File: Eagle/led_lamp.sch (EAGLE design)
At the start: 7 parts

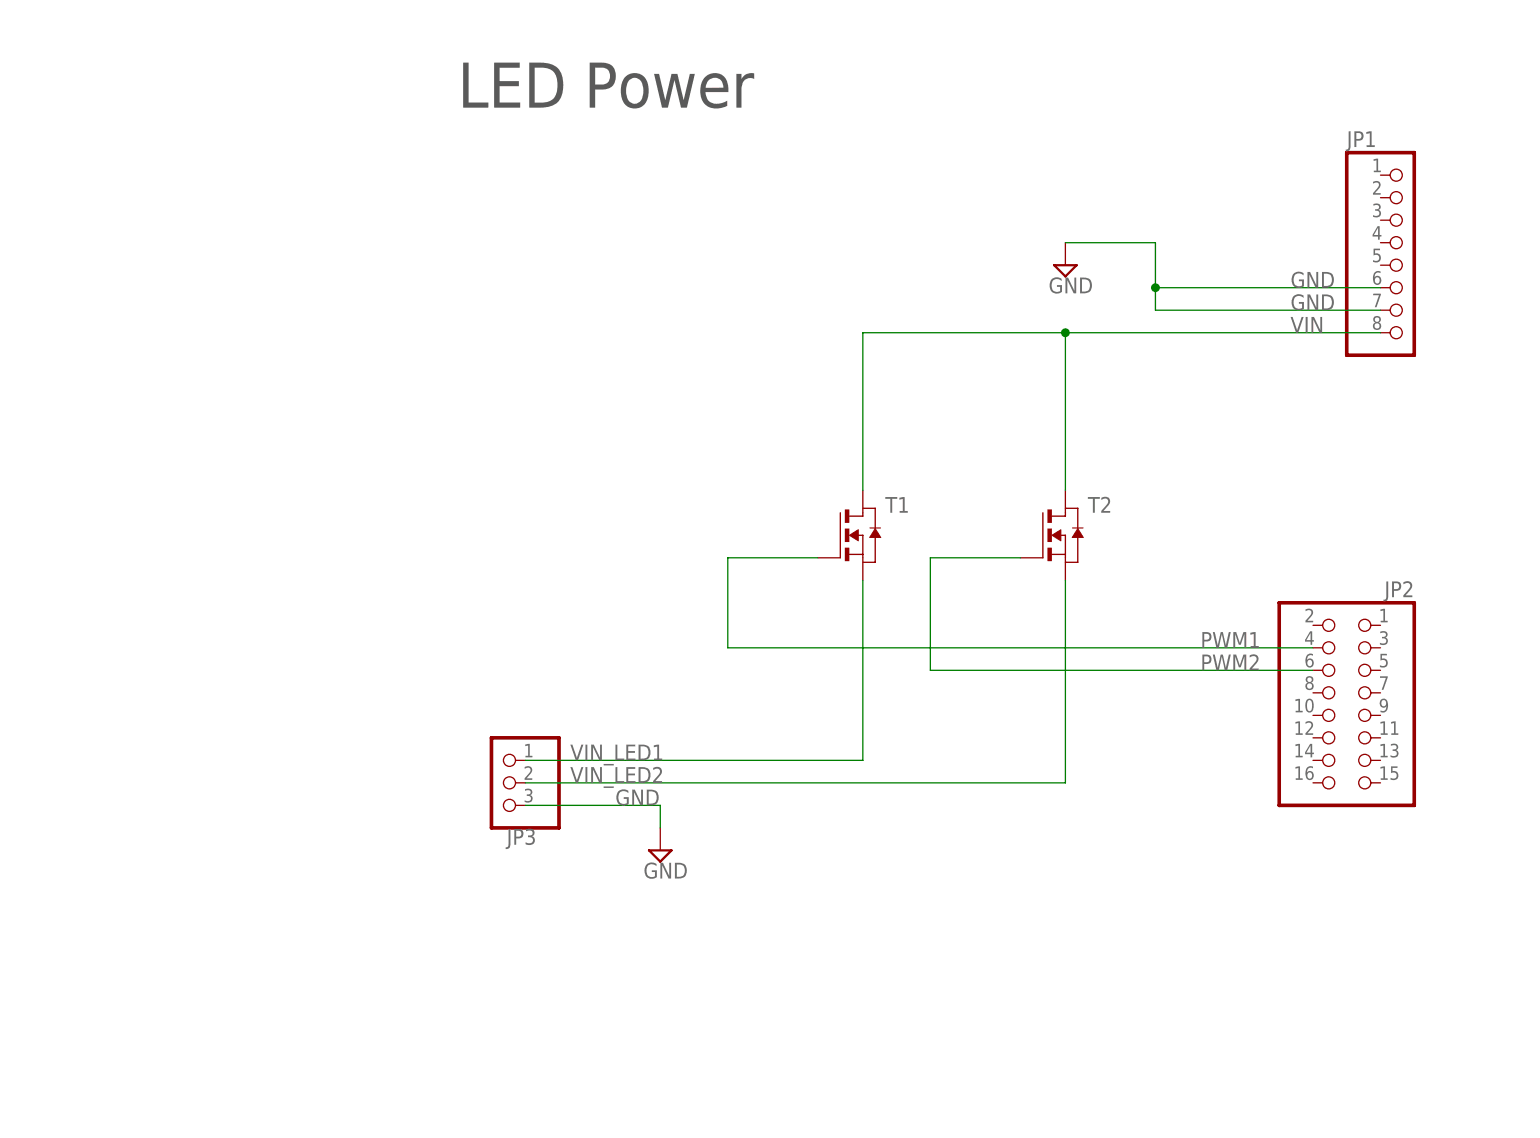
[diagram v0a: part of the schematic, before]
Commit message: Updated arduino project and eagle project
Eagle:
- Added push button along with auxiliary componetns

Arduino Project
- Added profiles
- Added serial command to set both LEDs with one command
- Merged seperate set_led functions into one
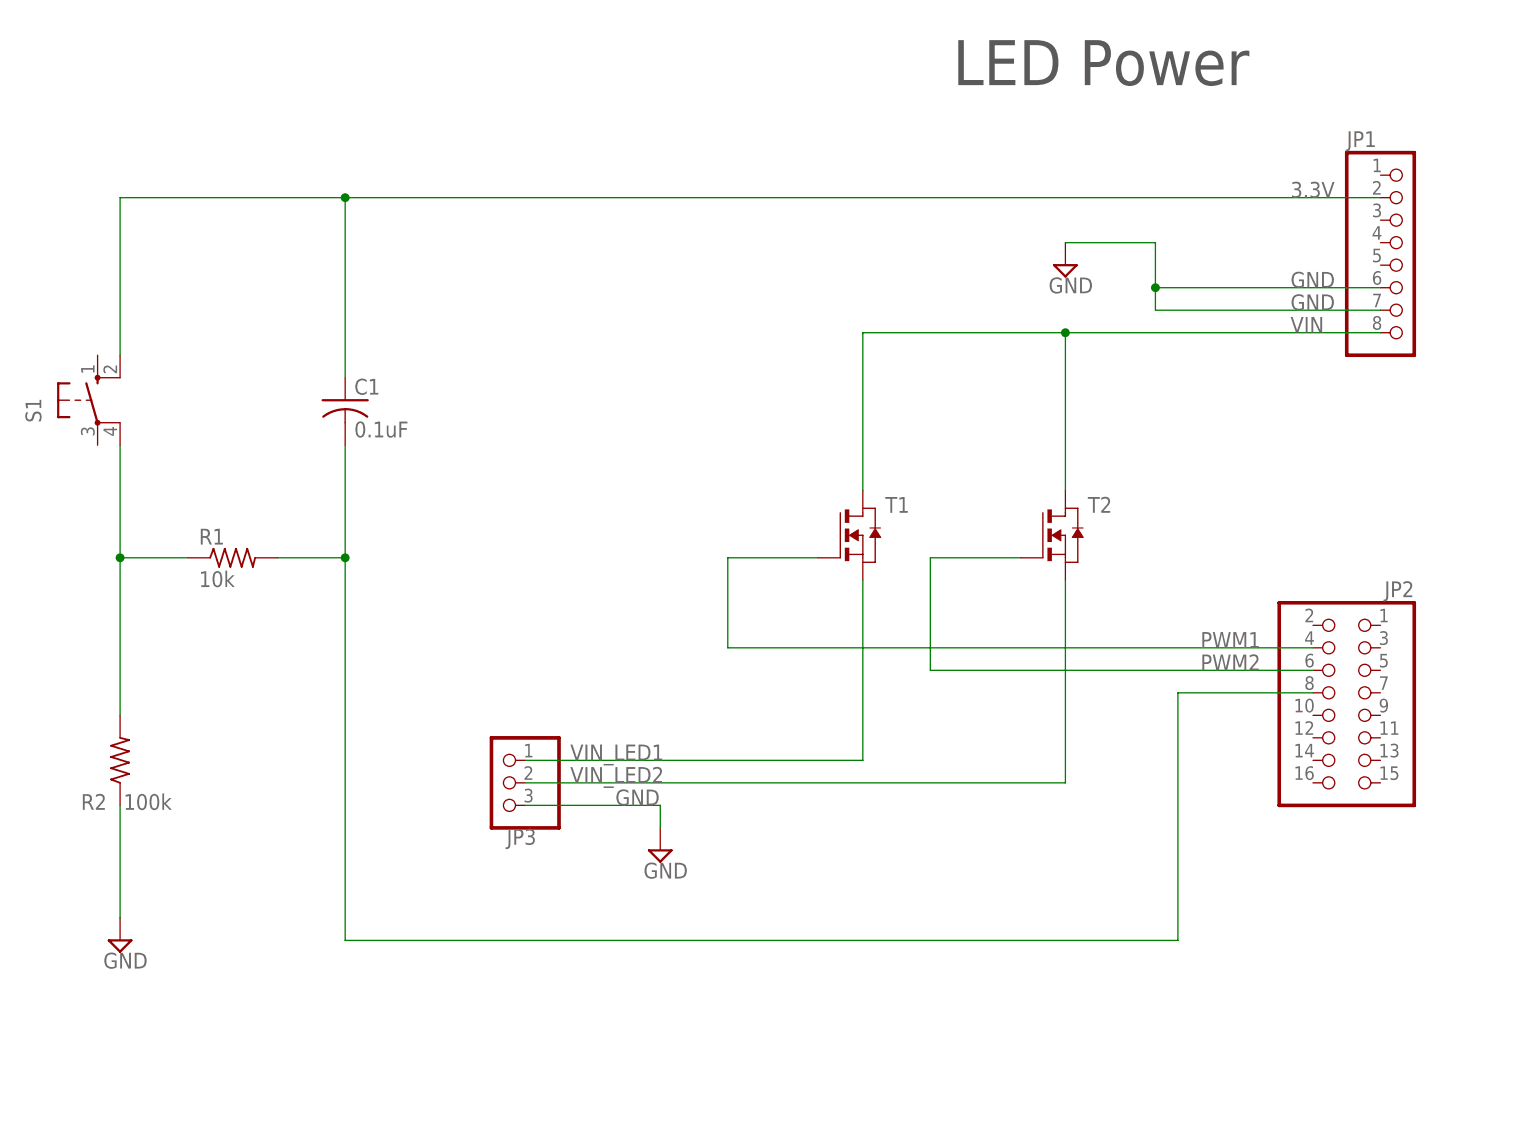
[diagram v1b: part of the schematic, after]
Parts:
- added C1: 0.1uF, rcl:C-USC1206K
- added R1: 10k, rcl:R-US_R1206
- added R2: 100k, rcl:R-US_R1206
- added S1: (no value), switch-omron:10-XX
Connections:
- new net 3.3V: C1.1, JP1.2, S1.S1
- new net N$1: R1.1, R2.2, S1.P1
- new net N$2: C1.2, JP2.8, R1.2
- net GND: now also R2.1
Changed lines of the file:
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@@
 <layers>
 <layer number="1" name="Top" color="4" fill="1" visible="no" active="no"/>
+<layer number="2" name="Route2" color="1" fill="3" visible="no" active="no"/>
+<layer number="3" name="Route3" color="4" fill="3" visible="no" active="no"/>
+<layer number="4" name="Route4" color="1" fill="4" visible="no" active="no"/>
+<layer number="5" name="Route5" color="4" fill="4" visible="no" active="no"/>
+<layer number="6" name="Route6" color="1" fill="8" visible="no" active="no"/>
+<layer number="7" name="Route7" color="4" fill="8" visible="no" active="no"/>
+<layer number="8" name="Route8" color="1" fill="2" visible="no" active="no"/>
+<layer number="9" name="Route9" color="4" fill="2" visible="no" active="no"/>
+<layer number="10" name="Route10" color="1" fill="7" visible="no" active="no"/>
+<layer number="11" name="Route11" color="4" fill="7" visible="no" active="no"/>
+<layer number="12" name="Route12" color="1" fill="5" visible="no" active="no"/>
+<layer number="13" name="Route13" color="4" fill="5" visible="no" active="no"/>
+<layer number="14" name="Route14" color="1" fill="6" visible="no" active="no"/>
+<layer number="15" name="Route15" color="4" fill="6" visible="no" active="no"/>
 <layer number="16" name="Bottom" color="1" fill="1" visible="no" active="no"/>
 <layer number="17" name="Pads" color="2" fill="1" visible="no" active="no"/>
@@
 <part name="SUPPLY2" library="supply2" library_urn="urn:adsk.eagle:library:372" deviceset="GND" device=""/>
 <part name="SUPPLY3" library="supply2" library_urn="urn:adsk.eagle:library:372" deviceset="GND" device=""/>
+<part name="S1" library="switch-omron" library_urn="urn:adsk.eagle:library:377" deviceset="10-XX" device="" package3d_urn="urn:adsk.eagle:package:27496/1"/>
+<part name="R1" library="rcl" library_urn="urn:adsk.eagle:library:334" deviceset="R-US_" device="R1206" package3d_urn="urn:adsk.eagle:package:23540/2" value="10k"/>
+<part name="R2" library="rcl" library_urn="urn:adsk.eagle:library:334" deviceset="R-US_" device="R1206" package3d_urn="urn:adsk.eagle:package:23540/2" value="100k"/>
+<part name="C1" library="rcl" library_urn="urn:adsk.eagle:library:334" deviceset="C-US" device="C1206K" package3d_urn="urn:adsk.eagle:package:23682/2" value="0.1uF"/>
+<part name="SUPPLY4" library="supply2" library_urn="urn:adsk.eagle:library:372" deviceset="GND" device=""/>
 </parts>
 <sheets>
@@
 <text x="266.7" y="7.62" size="2.54" layer="94" font="vector">A</text>
 <text x="183.896" y="1.27" size="2.54" layer="94" font="vector">March 1, 2019</text>
-<text x="76.2" y="193.04" size="5.08" layer="97">LED Power</text>
+<text x="132.08" y="195.58" size="5.08" layer="97">LED Power</text>
 <text x="205.74" y="193.04" size="5.08" layer="97">I2C Passthrough</text>
 </plain>
@@
 <instance part="SUPPLY3" gate="GND" x="144.78" y="175.26" smashed="yes">
 <attribute name="VALUE" x="142.875" y="172.085" size="1.778" layer="96"/>
+</instance>
+<instance part="S1" gate="1" x="35.56" y="160.02" smashed="yes">
+<attribute name="NAME" x="29.21" y="157.48" size="1.778" layer="95" rot="R90"/>
+<attribute name="VALUE" x="31.75" y="163.195" size="1.778" layer="96" rot="R90"/>
+</instance>
+<instance part="R1" gate="G$1" x="50.8" y="142.24" smashed="yes">
+<attribute name="NAME" x="46.99" y="143.7386" size="1.778" layer="95"/>
+<attribute name="VALUE" x="46.99" y="138.938" size="1.778" layer="96"/>
+</instance>
+<instance part="R2" gate="G$1" x="38.1" y="119.38" smashed="yes" rot="R90">
+<attribute name="NAME" x="36.6014" y="115.57" size="1.778" layer="95" rot="R180"/>
+<attribute name="VALUE" x="43.942" y="115.57" size="1.778" layer="96" rot="R180"/>
+</instance>
+<instance part="C1" gate="G$1" x="63.5" y="160.02" smashed="yes">
+<attribute name="NAME" x="64.516" y="160.655" size="1.778" layer="95"/>
+<attribute name="VALUE" x="64.516" y="155.829" size="1.778" layer="96"/>
+</instance>
+<instance part="SUPPLY4" gate="GND" x="38.1" y="99.06" smashed="yes">
+<attribute name="VALUE" x="36.195" y="95.885" size="1.778" layer="96"/>
 </instance>
 </instances>
@@
 <junction x="154.94" y="172.72"/>
 </segment>
+<segment>
+<pinref part="R2" gate="G$1" pin="1"/>
+<pinref part="SUPPLY4" gate="GND" pin="GND"/>
+<wire x1="38.1" y1="114.3" x2="38.1" y2="101.6" width="0.1524" layer="91"/>
+</segment>
 </net>
 <net name="VIN" class="0">
@@
 <wire x1="246.38" y1="170.18" x2="218.44" y2="170.18" width="0.1524" layer="91"/>
 <label x="236.22" y="170.18" size="1.778" layer="95"/>
+</segment>
+</net>
+<net name="N$1" class="0">
+<segment>
+<pinref part="S1" gate="1" pin="P1"/>
+<wire x1="38.1" y1="154.94" x2="38.1" y2="142.24" width="0.1524" layer="91"/>
+<pinref part="R1" gate="G$1" pin="1"/>
+<wire x1="38.1" y1="142.24" x2="45.72" y2="142.24" width="0.1524" layer="91"/>
+<pinref part="R2" gate="G$1" pin="2"/>
+<wire x1="38.1" y1="124.46" x2="38.1" y2="142.24" width="0.1524" layer="91"/>
+<junction x="38.1" y="142.24"/>
+</segment>
+</net>
+<net name="N$2" class="0">
+<segment>
+<pinref part="R1" gate="G$1" pin="2"/>
+<pinref part="C1" gate="G$1" pin="2"/>
+<wire x1="55.88" y1="142.24" x2="63.5" y2="142.24" width="0.1524" layer="91"/>
+<wire x1="63.5" y1="142.24" x2="63.5" y2="154.94" width="0.1524" layer="91"/>
+<wire x1="63.5" y1="142.24" x2="63.5" y2="99.06" width="0.1524" layer="91"/>
+<junction x="63.5" y="142.24"/>
+<wire x1="63.5" y1="99.06" x2="157.48" y2="99.06" width="0.1524" layer="91"/>
+<pinref part="JP2" gate="A" pin="8"/>
+<wire x1="157.48" y1="99.06" x2="157.48" y2="127" width="0.1524" layer="91"/>
+<wire x1="157.48" y1="127" x2="172.72" y2="127" width="0.1524" layer="91"/>
+</segment>
+</net>
+<net name="3.3V" class="0">
+<segment>
+<pinref part="S1" gate="1" pin="S1"/>
+<wire x1="38.1" y1="165.1" x2="38.1" y2="182.88" width="0.1524" layer="91"/>
+<wire x1="38.1" y1="182.88" x2="63.5" y2="182.88" width="0.1524" layer="91"/>
+<pinref part="C1" gate="G$1" pin="1"/>
+<wire x1="63.5" y1="182.88" x2="63.5" y2="162.56" width="0.1524" layer="91"/>
+<pinref part="JP1" gate="A" pin="2"/>
+<wire x1="180.34" y1="182.88" x2="63.5" y2="182.88" width="0.1524" layer="91"/>
+<junction x="63.5" y="182.88"/>
+<label x="170.18" y="182.88" size="1.778" layer="95"/>
 </segment>
 </net>
@@
 packages will not be understood (or retained) with this version.
 </note>
+<note version="8.4" severity="warning">
+Since Version 8.4, EAGLE supports properties for SPICE simulation.
+Probes in schematics and SPICE mapping objects found in parts and library devices
+will not be understood with this version. Update EAGLE to the latest version
+for full support of SPICE simulation.
+</note>
 </compatibility>
